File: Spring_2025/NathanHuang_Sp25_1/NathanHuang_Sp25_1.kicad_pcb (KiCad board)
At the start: 2 copper layers, 13 parts, among them J1 Barrel_Jack, M1 Motor_Servo, M2 Motor_Servo, M3 Motor_Servo, M4 Motor_Servo, M5 Motor_Servo, M6 Motor_Servo, M7 Stepper_Motor_bipolar, U1 ESP32-DEVKITC-32UE, U2 LM2596_BUCK_CONVERTER

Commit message: PCB Changes
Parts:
- removed the J1 at (240.5, 53.5)
- removed the J1 at (274.5, 48.0)
- added J1: Barrel_Jack, Connector_BarrelJack:BarrelJack_SwitchcraftConxall_RAPC10U_Horizontal, F.Cu at (54.7, 41.5)
- moved C1 178.3 mm to (74.0, 41.0), turned to 180 degrees
- moved A1 171.6 mm to (57.2, 93.2), turned to 180 degrees
- moved M7 160.1 mm to (76.5, 86.0), turned to 180 degrees
- moved U2 156.0 mm to (123.1, 49.0), turned to 180 degrees
- moved U1 52.4 mm to (103.2, 95.9)
- moved M6 27.6 mm to (143.5, 119.5)
- moved M5 26.7 mm to (143.6, 110.5)
- moved M4 24.4 mm to (143.1, 100.0)
- moved M3 23.0 mm to (143.0, 89.5)
- moved M2 21.5 mm to (143.1, 76.5)
- moved M1 21.2 mm to (143.0, 64.0)
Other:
- board outline added: 139.5 x 109.5 mm
- board text added: "12 V Side"
- board text added: "7.2 V Side"

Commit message: Finished PCB, Ready for Print
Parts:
- added H1: MountingHole, MountingHole:MountingHole_2.1mm, F.Cu at (210.5, 48.5)
- added H2: MountingHole, MountingHole:MountingHole_2.1mm, F.Cu at (86.5, 48.5)
- added H3: MountingHole, MountingHole:MountingHole_2.1mm, F.Cu at (87.0, 138.0)
- added H4: MountingHole, MountingHole:MountingHole_2.1mm, F.Cu at (210.5, 141.0)
- moved J1 63.2 mm to (114.4, 62.2)
- moved U1 63.2 mm to (162.9, 116.6)
- moved M1 61.8 mm to (188.2, 106.2)
- moved M6 60.8 mm to (199.6, 96.0)
- moved M2 58.7 mm to (188.0, 114.2)
- moved A1 56.8 mm to (113.5, 100.6)
- moved M3 55.4 mm to (188.0, 121.7)
- moved M4 53.7 mm to (188.2, 129.2)
- moved M5 46.7 mm to (188.0, 96.2)
- moved M7 46.5 mm to (122.8, 89.7), turned to 0 degrees
- moved C1 41.0 mm to (114.4, 48.2)
- moved U2 19.2 mm to (142.2, 51.7), turned to 0 degrees
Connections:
- A1 pad 2: +5V -> +3V3
- M7 pad 1: Net-(A1-1B) -> Net-(A1-2B)
- M7 pad 2: Net-(A1-1A) -> Net-(A1-2A)
- M7 pad 3: Net-(A1-2A) -> Net-(A1-1A)
- M7 pad 4: Net-(A1-2B) -> Net-(A1-1B)
- U1 pad 1: unconnected-(U1-3V3-Pad1) -> +3V3
- U1 pad 12: /STEP_PIN -> unconnected-(U1-14-Pad12)
- U1 pad 13: /THUMB_1 -> unconnected-(U1-12-Pad13)
- U1 pad 15: /THUMB_2 -> unconnected-(U1-13-Pad15)
- U1 pad 19: +5V -> unconnected-(U1-5V-Pad19)
- U1 pad 21: unconnected-(U1-23-Pad21) -> /THUMB_1
- U1 pad 22: unconnected-(U1-Pad22) -> /THUMB_2
- U1 pad 25: unconnected-(U1-21-Pad25) -> /INDEX
- U1 pad 28: unconnected-(U1-18-Pad28) -> /MIDDLE
- U1 pad 29: /PINKIE -> unconnected-(U1-5-Pad29)
- U1 pad 31: unconnected-(U1-16-Pad31) -> /RING
- U1 pad 32: /RING -> unconnected-(U1-4-Pad32)
- U1 pad 33: /INDEX -> unconnected-(U1-0-Pad33)
- U1 pad 34: /MIDDLE -> /PINKIE
- U1 pad 35: /DIR_PIN -> unconnected-(U1-15-Pad35)
- U1 pad 6: unconnected-(U1-35-Pad6) -> /DIR_PIN
- U1 pad 7: unconnected-(U1-32-Pad7) -> /STEP_PIN
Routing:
- net GND: track 0.00 -> 344.3 mm
- net 7.2V: track 0.00 -> 125.7 mm
- net /STEP_PIN: track 0.00 -> 70.7 mm
- net +12V: track 0.00 -> 64.2 mm
- net /DIR_PIN: track 0.00 -> 63.5 mm
- net +3V3: track 0.00 -> 38.5 mm
- net /THUMB_2: track 0.00 -> 29.3 mm
- net /INDEX: track 0.00 -> 12.7 mm
- net /PINKIE: track 0.00 -> 12.6 mm
- net /MIDDLE: track 0.00 -> 12.5 mm
- net /RING: track 0.00 -> 12.5 mm
- net /THUMB_1: track 0.00 -> 12.5 mm
- net Net-(A1-1B): track 0.00 -> 10.4 mm
- net Net-(A1-2B): track 0.00 -> 10.0 mm
- net Net-(A1-1A): track 0.00 -> 9.81 mm
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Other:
- board size 139.5 x 109.5 mm -> 144 x 112.5 mm

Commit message: PCB Updates
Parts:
- added Encoder1: ~, Connector_PinHeader_2.54mm:PinHeader_1x04_P2.54mm_Horizontal, F.Cu at (147.1, 120.8)
- added SW1: SW_Push, Connector_PinHeader_2.54mm:PinHeader_1x02_P2.54mm_Horizontal, F.Cu at (147.1, 135.2)
- added SW2: SW_Push, Connector_PinHeader_2.54mm:PinHeader_1x02_P2.54mm_Horizontal, F.Cu at (147.1, 128.1)
- C1: footprint Capacitor_THT:CP_Radial_Tantal_D5.0mm_P2.50mm -> Capacitor_THT:CP_Radial_D4.0mm_P1.50mm
- H1, H2, H3, H4: footprint MountingHole:MountingHole_2.1mm -> MountingHole:MountingHole_5.3mm_M5
- M1, M2, M3, M4, M5, M6: footprint Connector_PinHeader_1.00mm:PinHeader_1x03_P1.00mm_Horizontal -> Connector_PinHeader_2.54mm:PinHeader_1x03_P2.54mm_Horizontal
- M7: footprint Connector_PinHeader_1.00mm:PinHeader_1x04_P1.00mm_Horizontal -> Connector_PinHeader_2.54mm:PinHeader_1x04_P2.54mm_Horizontal
- U1: value ESP32-DEVKITC-32UE -> ESP32-WROOM-32; footprint Library:ESP32-DEVKITC-32UE -> RF_Module:ESP32-WROOM-32
- moved U2 121.7 mm to (25.0, 19.0)
- moved U1 63.6 mm to (151.3, 54.1)
- moved J1 19.1 mm to (95.6, 65.5)
- moved A1 11.9 mm to (101.8, 103.1)
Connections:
- U1 pad 1: +3V3 -> GND
- U1 pad 13: unconnected-(U1-12-Pad13) -> /DT
- U1 pad 14: GND -> /PINKIE
- U1 pad 15: unconnected-(U1-13-Pad15) -> GND
- U1 pad 16: unconnected-(U1-D2-Pad16) -> /CW
- U1 pad 2: unconnected-(U1-EN-Pad2) -> +3V3
- U1 pad 21: /THUMB_1 -> unconnected-(U1-SDO/SD0-Pad21)
- U1 pad 22: /THUMB_2 -> unconnected-(U1-SDI/SD1-Pad22)
- U1 pad 23: unconnected-(U1-TX-Pad23) -> /RING
- U1 pad 25: /INDEX -> Net-(U1-IO0)
- U1 pad 26: GND -> Net-(U1-IO4)
- U1 pad 27: unconnected-(U1-19-Pad27) -> /MIDDLE
- U1 pad 28: /MIDDLE -> /INDEX
- U1 pad 30: unconnected-(U1-17-Pad30) -> /THUMB_2
- U1 pad 31: /RING -> /THUMB_1
- U1 pad 33: unconnected-(U1-0-Pad33) -> /STEP_PIN
- U1 pad 34: /PINKIE -> unconnected-(U1-RXD0/IO3-Pad34)
- U1 pad 36: unconnected-(U1-D1-Pad36) -> /DIR_PIN
- U1 pad 38: unconnected-(U1-CLK-Pad38) -> GND
- U1 pad 6: /DIR_PIN -> unconnected-(U1-IO34-Pad6)
- U1 pad 7: /STEP_PIN -> unconnected-(U1-IO35-Pad7)
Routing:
- net GND: track 344.3 -> 0.00 mm
- net 7.2V: track 125.7 -> 0.00 mm
- net /STEP_PIN: track 70.7 -> 0.00 mm
- net +12V: track 64.2 -> 0.00 mm
- net /DIR_PIN: track 63.5 -> 0.00 mm
- net +3V3: track 38.5 -> 0.00 mm
- net /THUMB_2: track 29.3 -> 0.00 mm
- net /INDEX: track 12.7 -> 0.00 mm
- net /PINKIE: track 12.6 -> 0.00 mm
- net /MIDDLE: track 12.5 -> 0.00 mm
- net /RING: track 12.5 -> 0.00 mm
- net /THUMB_1: track 12.5 -> 0.00 mm
- net Net-(A1-1B): track 10.4 -> 0.00 mm
- net Net-(A1-2B): track 10.0 -> 0.00 mm
- net Net-(A1-1A): track 9.81 -> 0.00 mm
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
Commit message: 4/4 Changes
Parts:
- moved U2 108.8 mm to (131.0, 43.4)
- moved U1 66.6 mm to (204.7, 93.9), turned to -90 degrees
- moved M4 66.0 mm to (122.9, 138.7), turned to -90 degrees
- moved M3 55.4 mm to (135.3, 138.7), turned to -90 degrees
- moved M6 50.6 mm to (172.4, 138.7), turned to -90 degrees
- moved M2 47.2 mm to (147.7, 138.7), turned to -90 degrees
- moved M1 43.0 mm to (160.0, 138.7), turned to -90 degrees
- moved M5 42.6 mm to (184.8, 138.7), turned to -90 degrees
- moved Encoder1 35.4 mm to (164.0, 89.7), turned to 90 degrees
- moved SW2 31.2 mm to (176.1, 116.5), turned to -90 degrees
- moved J1 26.0 mm to (95.1, 91.5)
- moved SW1 25.4 mm to (164.6, 116.8), turned to -90 degrees
- moved A1 24.5 mm to (126.3, 104.7), turned to -90 degrees
- moved M7 9.10 mm to (113.7, 89.8), turned to 90 degrees
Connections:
- Encoder1 pad 1: (no net) -> /DT
- Encoder1 pad 2: (no net) -> /CW
- Encoder1 pad 3: (no net) -> +3V3
- Encoder1 pad 4: (no net) -> GND
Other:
- board text added: "12 V OPERATION"
- board text added: "7.2 V OPERATION"
- board text removed: "12 V Side"
- board text removed: "7.2 V Side"

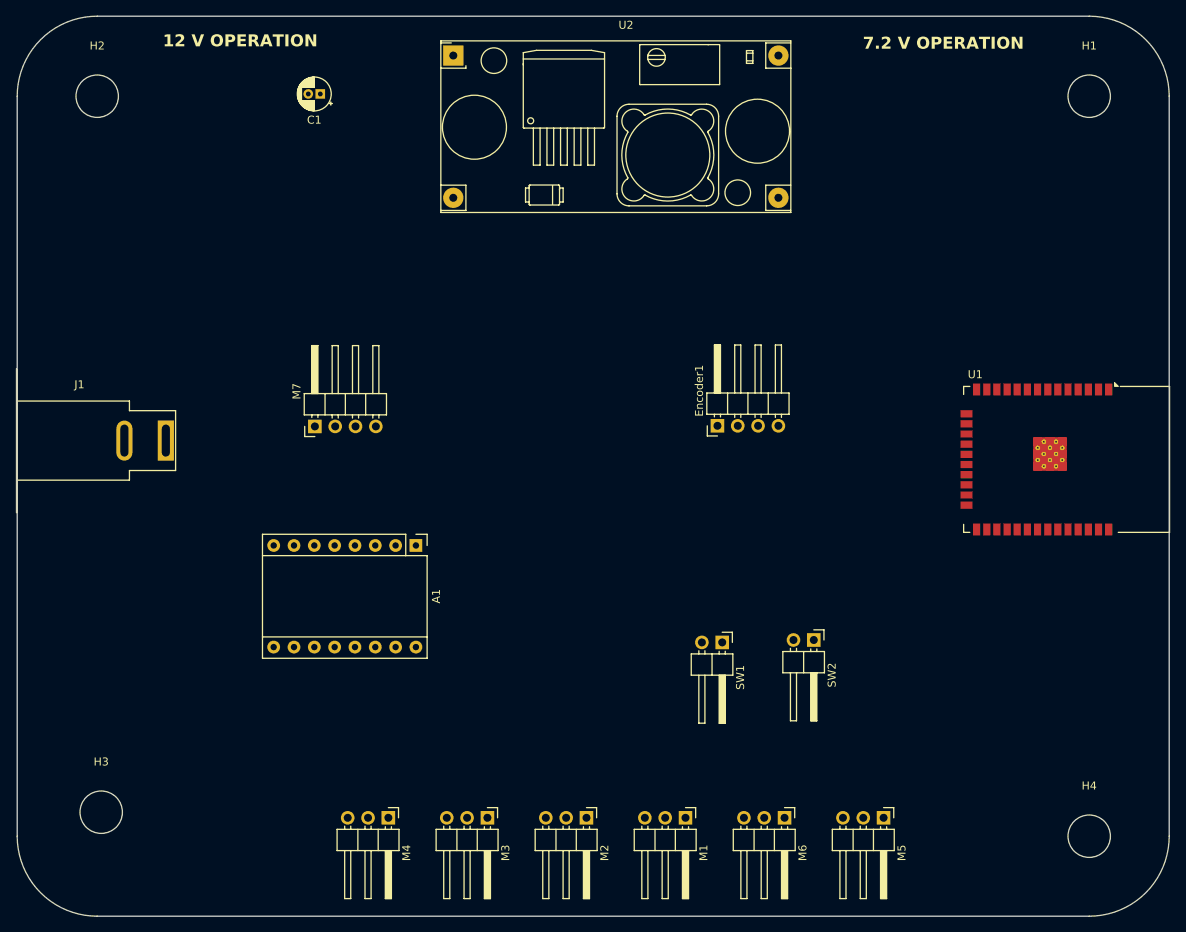
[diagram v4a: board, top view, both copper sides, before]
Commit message: Found Footprint
New to find new schematic for 30 pin
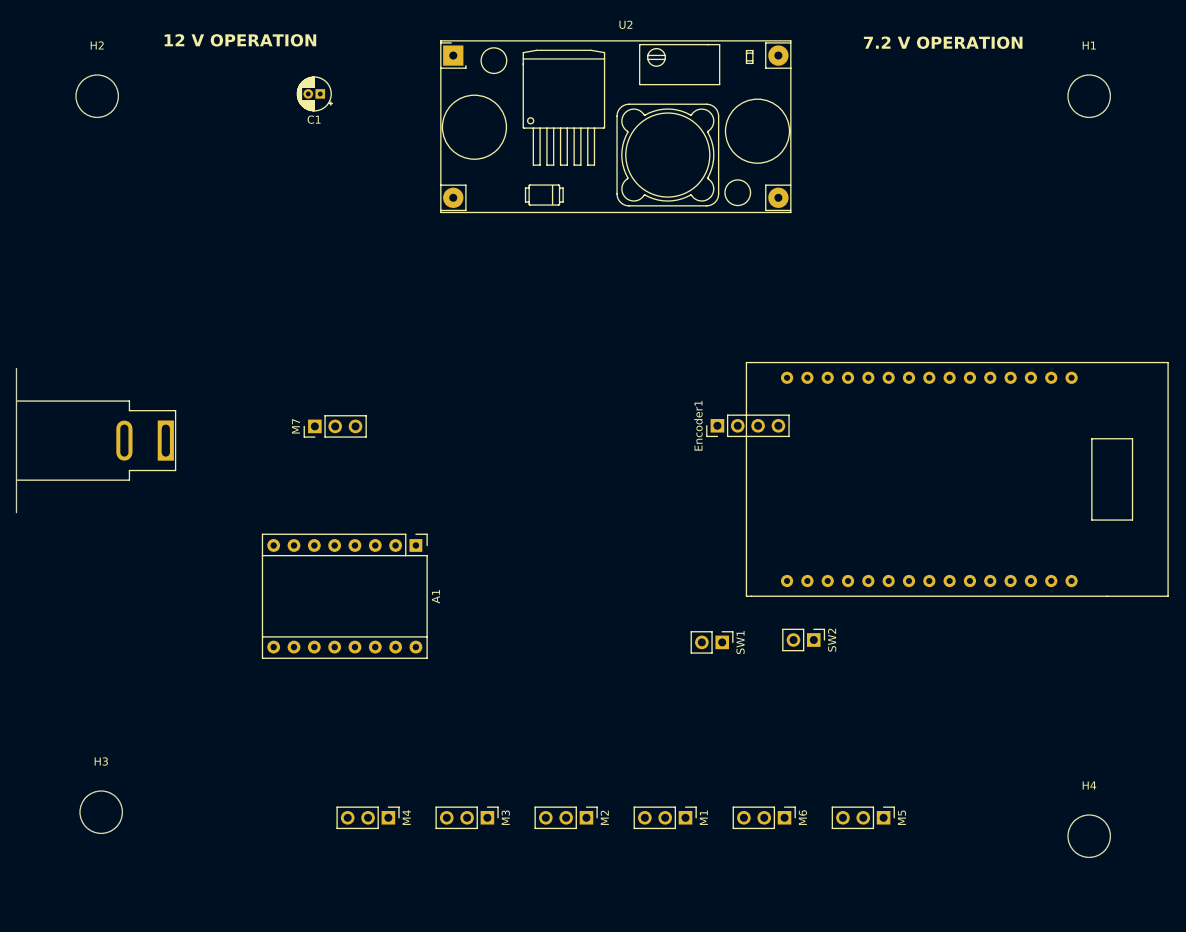
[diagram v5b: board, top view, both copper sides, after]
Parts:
- Encoder1: footprint Connector_PinHeader_2.54mm:PinHeader_1x04_P2.54mm_Horizontal -> Connector_PinHeader_2.54mm:PinHeader_1x04_P2.54mm_Vertical
- M1, M2, M3, M4, M5, M6: footprint Connector_PinHeader_2.54mm:PinHeader_1x03_P2.54mm_Horizontal -> Connector_PinHeader_2.54mm:PinHeader_1x03_P2.54mm_Vertical
- M7: footprint Connector_PinHeader_2.54mm:PinHeader_1x04_P2.54mm_Horizontal -> Connector_PinHeader_2.54mm:PinHeader_1x03_P2.54mm_Vertical
- SW1, SW2: footprint Connector_PinHeader_2.54mm:PinHeader_1x02_P2.54mm_Horizontal -> Connector_PinHeader_2.54mm:PinHeader_1x02_P2.54mm_Vertical
- U1: footprint RF_Module:ESP32-WROOM-32 -> Library:ESP32-WROOM-32
- moved U1 42.4 mm to (165.1, 109.1), turned to 90 degrees
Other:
- board outline removed

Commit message: Overwrite Changes
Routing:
- added copper zone on B.Cu, net GND

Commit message: Changes
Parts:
- removed U1: ESP32-WROOM-32, Library:ESP32-WROOM-32
- added U3: ESP32-WROOM-32, Library:ESP32-WROOM-32, F.Cu at (381.2, 83.3)
- M7: footprint Connector_PinHeader_2.54mm:PinHeader_1x03_P2.54mm_Vertical -> Connector_PinHeader_2.54mm:PinHeader_1x04_P2.54mm_Vertical
- moved H2 306.8 mm to (392.9, 63.2)
- moved M4 220.1 mm to (331.9, 69.6)
- moved Encoder1 211.8 mm to (374.8, 69.6), turned to -90 degrees
- moved SW1 210.5 mm to (374.2, 136.5), turned to 180 degrees
- moved M6 199.6 mm to (359.7, 69.6)
- moved J1 196.2 mm to (288.8, 122.8), turned to 90 degrees
- moved M3 195.3 mm to (318.0, 69.6)
- moved SW2 191.0 mm to (366.0, 136.2), turned to 180 degrees
- moved U2 190.4 mm to (304.0, 123.1)
- moved H4 186.1 mm to (396.6, 137.5)
- moved C1 179.2 mm to (276.4, 124.7), turned to -90 degrees
- moved M5 175.2 mm to (345.8, 69.6)
- moved M2 171.0 mm to (304.1, 69.6)
- moved H3 166.6 mm to (253.6, 134.1)
- moved M7 161.1 mm to (274.4, 102.2), turned to 180 degrees
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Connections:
- Encoder1 pad 1: /DT -> GND
- Encoder1 pad 2: /CW -> +3V3
- Encoder1 pad 3: +3V3 -> /CW
- Encoder1 pad 4: GND -> /DT
- M1 pad 1: /INDEX -> /THUMB_1
- M2 pad 1: /MIDDLE -> /THUMB_2
- M3 pad 1: /RING -> /INDEX
- M4 pad 1: /PINKIE -> /MIDDLE
- M5 pad 1: /THUMB_1 -> /RING
- M6 pad 1: /THUMB_2 -> /PINKY
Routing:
- removed copper zone on B.Cu, net GND

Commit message: Don't clone
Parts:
- moved SW2 70.7 mm to (383.5, 67.6), turned to 90 degrees
- moved SW1 69.7 mm to (370.2, 66.9), turned to 90 degrees
- moved Encoder1 62.7 mm to (376.9, 132.3)
- moved U3 57.0 mm to (331.5, 111.1), turned to 90 degrees
- moved H2 9.83 mm to (402.7, 62.0)
